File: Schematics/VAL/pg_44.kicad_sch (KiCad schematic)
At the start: 10 parts

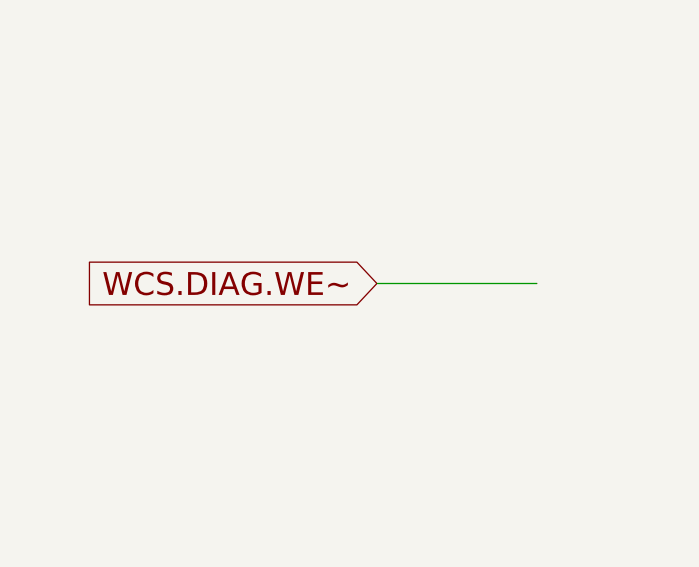
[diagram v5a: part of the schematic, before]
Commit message: SEQ+VAL polish.  Tested to 4.75s
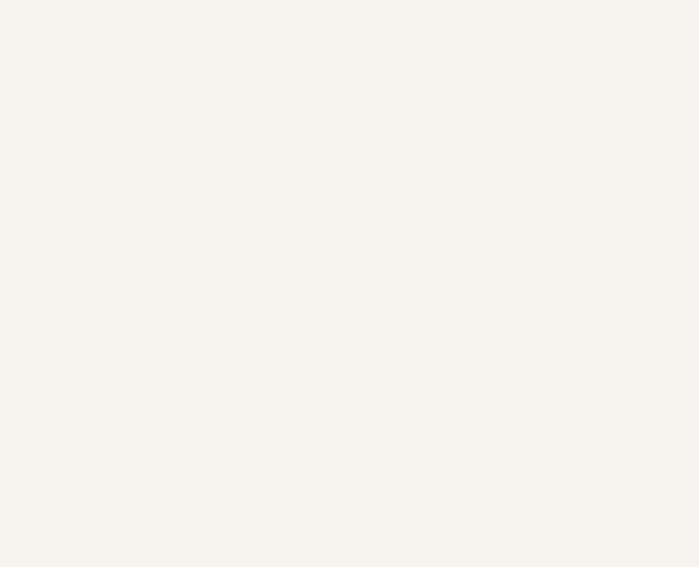
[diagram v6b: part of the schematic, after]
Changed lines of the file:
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@@
-    (stroke (width 0) (type default))
-  )
-  (wire (pts (xy 60.96 88.9) (xy 78.74 88.9))
     (stroke (width 0) (type default))
   )
@@
       (effects (font (size 1.905 1.905)) (justify right))
     )
-  )
-  (global_label "WCS.DIAG.WE~" (shape input) (at 60.96 88.9 180) (fields_autoplaced)
-    (effects (font (size 2.54 2.54)) (justify right))
-    (property "Intersheet References" "${INTERSHEET_REFS}" (id 0) (at 30.3711 88.7413 0)
-      (effects (font (size 1.905 1.905)) (justify right))
-    )

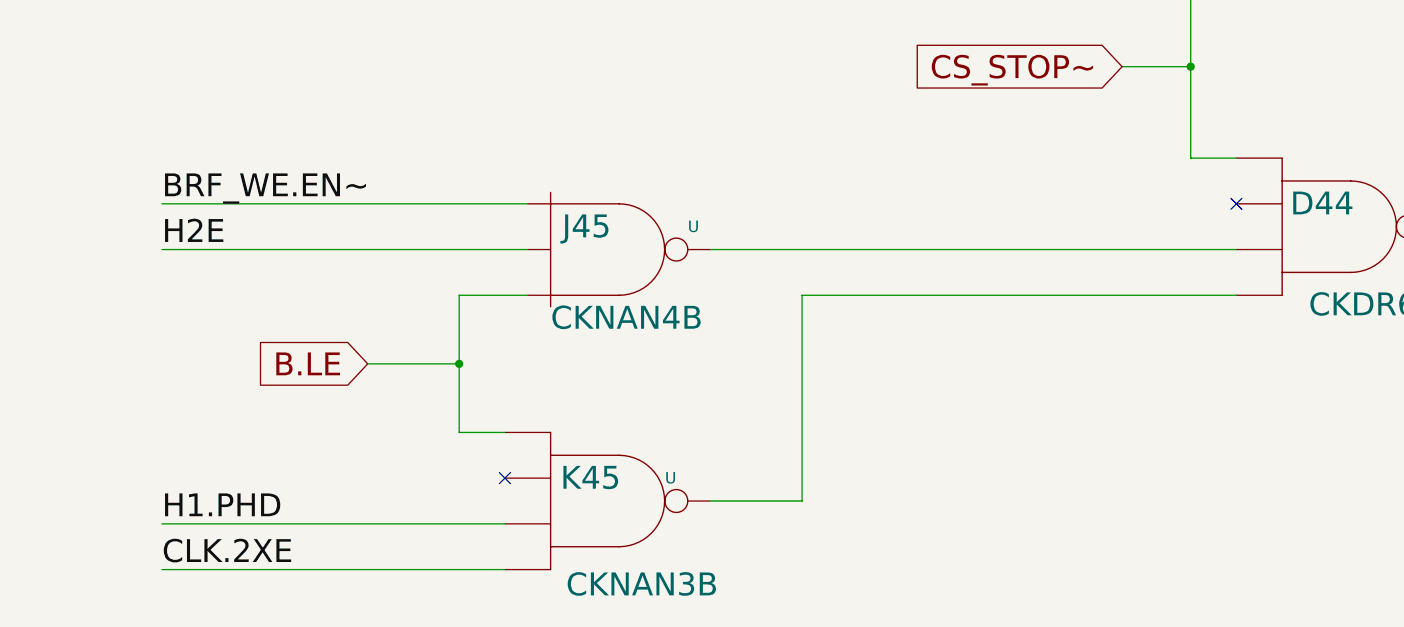
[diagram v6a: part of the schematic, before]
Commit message: TYP: Smarter RF-B, tested to 3.33s (rc046)
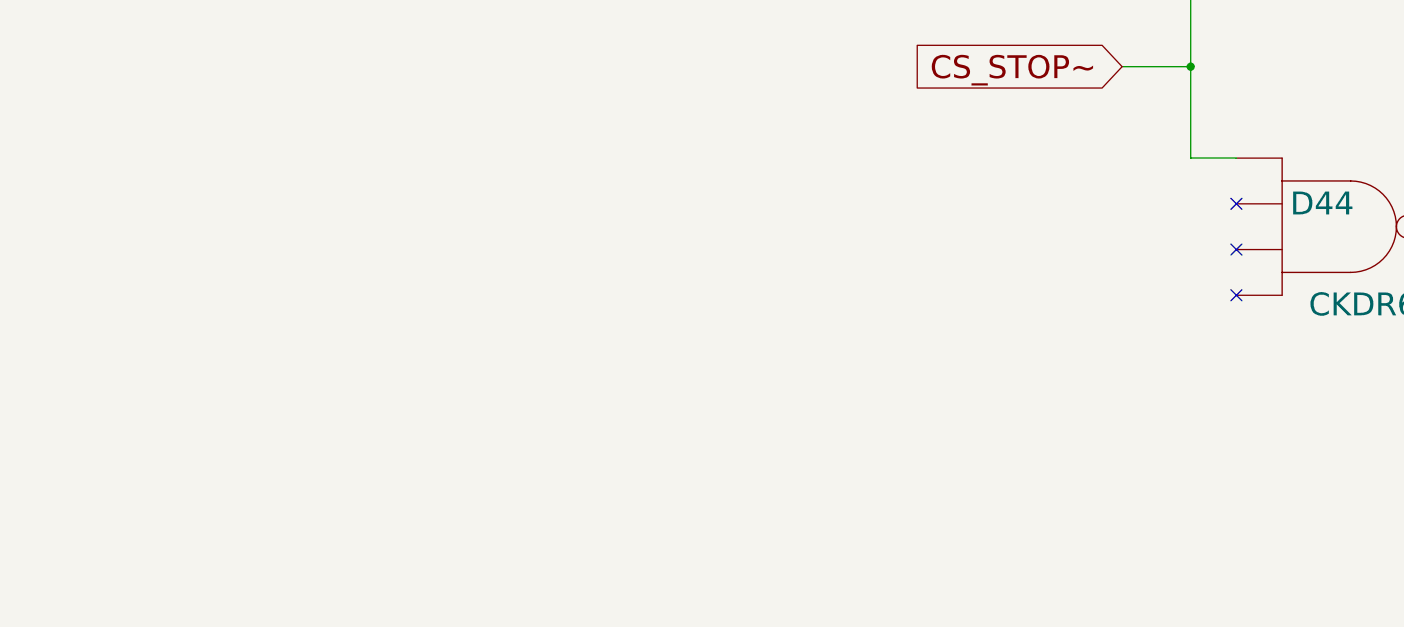
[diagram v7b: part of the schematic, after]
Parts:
- removed U: (no value), symbol r1000:F20
- removed U: (no value), symbol r1000:F10
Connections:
- no-connect marks 6 -> 7
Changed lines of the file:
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@@
   (junction (at 274.32 139.7) (diameter 0) (color 0 0 0 0)
   )
-  (junction (at 193.04 172.72) (diameter 0) (color 0 0 0 0)
-  )
   (junction (at 182.88 40.64) (diameter 0) (color 0 0 0 0)
   )
@@
   )
   (no_connect (at 269.24 27.94))
-  (no_connect (at 198.12 185.42))
+  (no_connect (at 279.4 160.02))
+  (no_connect (at 279.4 165.1))
   (no_connect (at 269.24 53.34))
   (no_connect (at 279.4 154.94))
@@
     (stroke (width 0) (type default))
   )
-  (wire (pts (xy 160.02 190.5) (xy 198.12 190.5))
-    (stroke (width 0) (type default))
-  )
   (wire (pts (xy 60.96 33.02) (xy 78.74 33.02))
     (stroke (width 0) (type default))
   )
-  (wire (pts (xy 193.04 165.1) (xy 200.66 165.1))
-    (stroke (width 0) (type default))
-  )
   (wire (pts (xy 220.98 58.42) (xy 269.24 58.42))
     (stroke (width 0) (type default))
   )
-  (wire (pts (xy 220.98 187.96) (xy 231.14 187.96))
-    (stroke (width 0) (type default))
-  )
   (wire (pts (xy 60.96 43.18) (xy 78.74 43.18))
     (stroke (width 0) (type default))
@@
     (stroke (width 0) (type default))
   )
-  (wire (pts (xy 193.04 165.1) (xy 193.04 172.72))
-    (stroke (width 0) (type default))
-  )
   (wire (pts (xy 264.16 43.18) (xy 264.16 40.64))
     (stroke (width 0) (type default))
@@
     (stroke (width 0) (type default))
   )
-  (wire (pts (xy 160.02 160.02) (xy 200.66 160.02))
-    (stroke (width 0) (type default))
-  )
   (wire (pts (xy 274.32 129.54) (xy 274.32 139.7))
     (stroke (width 0) (type default))
@@
     (stroke (width 0) (type default))
   )
-  (wire (pts (xy 193.04 180.34) (xy 198.12 180.34))
-    (stroke (width 0) (type default))
-  )
   (wire (pts (xy 302.26 157.48) (xy 309.88 157.48))
     (stroke (width 0) (type default))
@@
     (stroke (width 0) (type default))
   )
-  (wire (pts (xy 231.14 187.96) (xy 231.14 165.1))
-    (stroke (width 0) (type default))
-  )
   (wire (pts (xy 264.16 38.1) (xy 269.24 38.1))
     (stroke (width 0) (type default))
   )
-  (wire (pts (xy 220.98 160.02) (xy 279.4 160.02))
-    (stroke (width 0) (type default))
-  )
-  (wire (pts (xy 160.02 195.58) (xy 198.12 195.58))
-    (stroke (width 0) (type default))
-  )
   (wire (pts (xy 160.02 121.92) (xy 198.12 121.92))
     (stroke (width 0) (type default))
   )
-  (wire (pts (xy 231.14 165.1) (xy 279.4 165.1))
-    (stroke (width 0) (type default))
-  )
-  (wire (pts (xy 182.88 172.72) (xy 193.04 172.72))
-    (stroke (width 0) (type default))
-  )
   (wire (pts (xy 60.96 48.26) (xy 78.74 48.26))
     (stroke (width 0) (type default))
@@
     (stroke (width 0) (type default))
   )
-  (wire (pts (xy 200.66 154.94) (xy 160.02 154.94))
-    (stroke (width 0) (type default))
-  )
-  (wire (pts (xy 193.04 172.72) (xy 193.04 180.34))
-    (stroke (width 0) (type default))
-  )
   (wire (pts (xy 292.1 30.48) (xy 299.72 30.48))
     (stroke (width 0) (type default))
@@
   )
   (label "H2E" (at 160.02 91.44 0) (fields_autoplaced)
-    (effects (font (size 2.54 2.54)) (justify left bottom))
-  )
-  (label "H2E" (at 160.02 160.02 0) (fields_autoplaced)
-    (effects (font (size 2.54 2.54)) (justify left bottom))
-  )
-  (label "BRF_WE.EN~" (at 160.02 154.94 0) (fields_autoplaced)
-    (effects (font (size 2.54 2.54)) (justify left bottom))
-  )
-  (label "CLK.2XE" (at 160.02 195.58 0) (fields_autoplaced)
-    (effects (font (size 2.54 2.54)) (justify left bottom))
-  )
-  (label "H1.PHD" (at 160.02 190.5 0) (fields_autoplaced)
     (effects (font (size 2.54 2.54)) (justify left bottom))
   )
@@
     (effects (font (size 2.54 2.54)) (justify right))
     (property "Intersheet References" "${INTERSHEET_REFS}" (id 0) (at 51.054 37.9413 0)
-      (effects (font (size 1.905 1.905)) (justify right))
-    )
-  )
-  (global_label "B.LE" (shape input) (at 182.88 172.72 180) (fields_autoplaced)
-    (effects (font (size 2.54 2.54)) (justify right))
-    (property "Intersheet References" "${INTERSHEET_REFS}" (id 0) (at 169.9502 172.8787 0)
       (effects (font (size 1.905 1.905)) (justify right))
     )
@@
       (effects (font (size 2.54 2.54)) (justify left))
     )
-    (pin "1")
-    (pin "2")
-    (pin "3")
-    (pin "4")
-  )
-  (symbol (lib_id "r1000:F20") (at 208.28 187.96 0) (unit 1)
-    (in_bom yes) (on_board yes)
-    (default_instance (reference "U") (unit 1) (value "") (footprint ""))
-    (property "Reference" "U" (id 0) (at 216.535 185.42 0)
-      (effects (font (size 1.27 1.27)))
-    )
-    (property "Value" "" (id 1) (at 207.645 190.5 0)
-      (effects (font (size 2.54 2.54)))
-    )
-    (property "Footprint" "" (id 2) (at 207.01 187.96 0)
-      (effects (font (size 1.27 1.27)) hide)
-    )
-    (property "Datasheet" "" (id 3) (at 207.01 187.96 0)
-      (effects (font (size 1.27 1.27)) hide)
-    )
-    (property "Location" "K45" (id 4) (at 207.645 185.42 0)
-      (effects (font (size 2.54 2.54)))
-    )
-    (property "Name" "CKNAN3B" (id 5) (at 213.36 198.755 0)
-      (effects (font (size 2.54 2.54)) (justify bottom))
-    )
-    (pin "1")
-    (pin "2")
-    (pin "4")
-    (pin "5")
-    (pin "6")
-  )
-  (symbol (lib_id "r1000:F10") (at 205.74 157.48 0) (unit 1)
-    (in_bom yes) (on_board yes)
-    (default_instance (reference "U") (unit 1) (value "") (footprint ""))
-    (property "Reference" "U" (id 0) (at 219.075 157.48 0)
-      (effects (font (size 1.27 1.27)))
-    )
-    (property "Value" "" (id 1) (at 211.455 162.56 0)
-      (effects (font (size 2.54 2.54)) (justify right))
-    )
-    (property "Footprint" "" (id 2) (at 205.74 142.875 0)
-      (effects (font (size 1.27 1.27)) hide)
-    )
-    (property "Datasheet" "" (id 3) (at 205.74 142.875 0)
-      (effects (font (size 1.27 1.27)) hide)
-    )
-    (property "Location" "J45" (id 4) (at 204.47 157.48 0)
-      (effects (font (size 2.54 2.54)) (justify left))
-    )
-    (property "Name" "CKNAN4B" (id 5) (at 203.2 167.64 0)
-      (effects (font (size 2.54 2.54)) (justify left))
-    )
